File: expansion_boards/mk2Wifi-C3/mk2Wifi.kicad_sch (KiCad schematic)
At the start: 28 parts, among them J0 TRIG_EXT, J2 USB_C_Receptacle_USB2.0_16P, J3 UART_EXT, J4 OLED, SW1 SW_Push, U1 ESP32-C3-MINI-1, U2 AP2112K-3.3

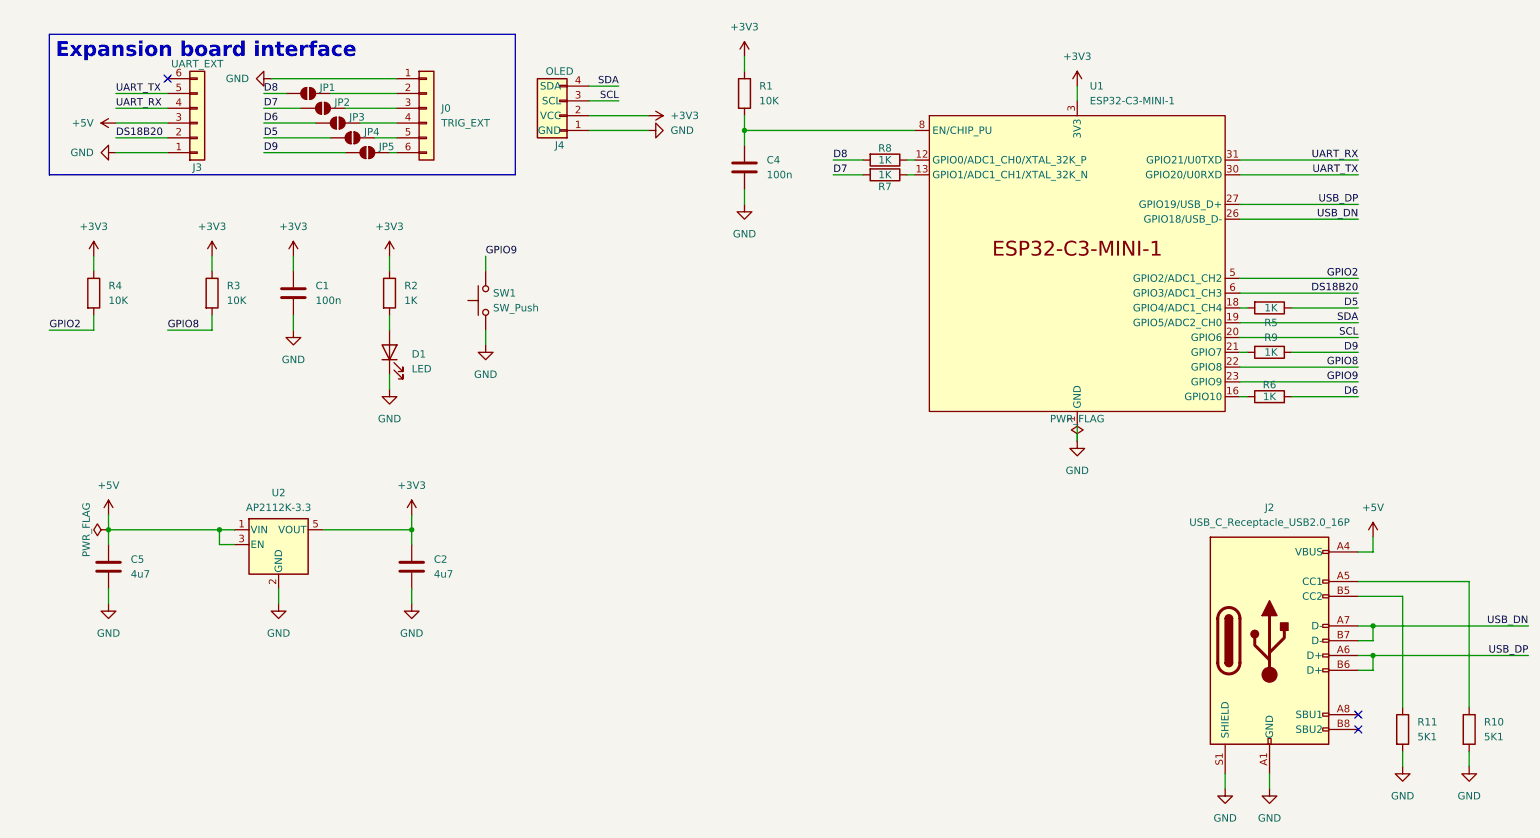
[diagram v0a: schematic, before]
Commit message: Add schematic descriptions and SVG exports to mk2Wifi READMEs
- Add title block comments (description, MCU, power, license) to both C3 and C6 schematics
- Rename C3 schematic title from "mk2Wifi" to "mk2Wifi-C3"
- Export schematic SVGs and add Schematic sections to all four READMEs

Co-Authored-By: Claude Opus 4.6 <noreply@anthropic.com>
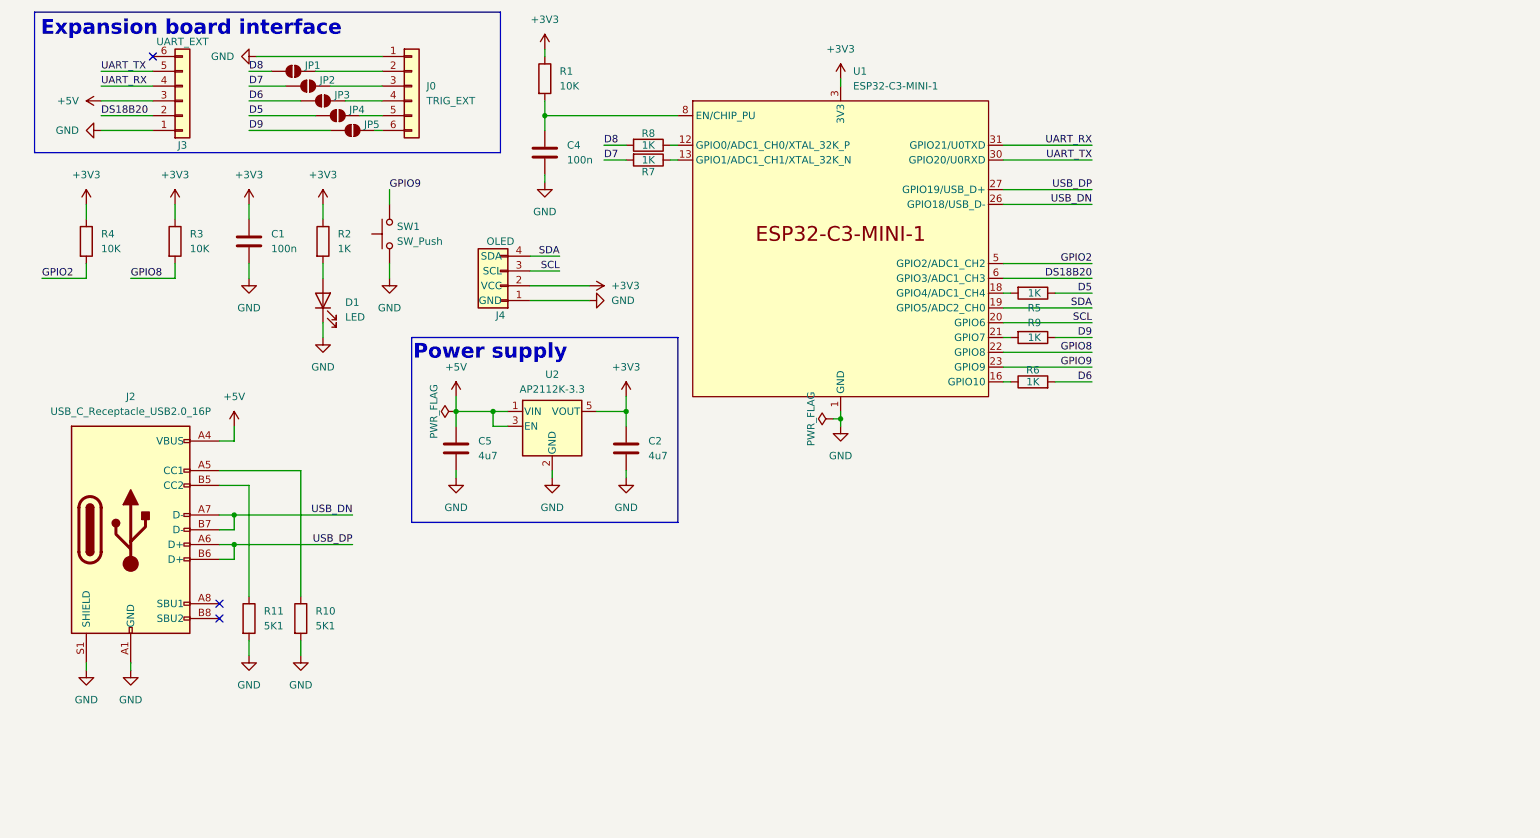
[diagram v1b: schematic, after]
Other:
- note added: "Power supply"
- title: mk2Wifi -> mk2Wifi-C3
- moved on the sheet: C1, C2, C4, C5, D1, J0, J2, J3, J4, JP1, JP2, JP3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
